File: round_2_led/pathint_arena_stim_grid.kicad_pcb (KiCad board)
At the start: 2 copper layers, 254 x 254 mm, 14 parts, among them J1 conn_2x13_odd_even, M1 0P25_THRU_HOLE, M2 0P25_THRU_HOLE, M3 0P25_THRU_HOLE, M4 0P25_THRU_HOLE

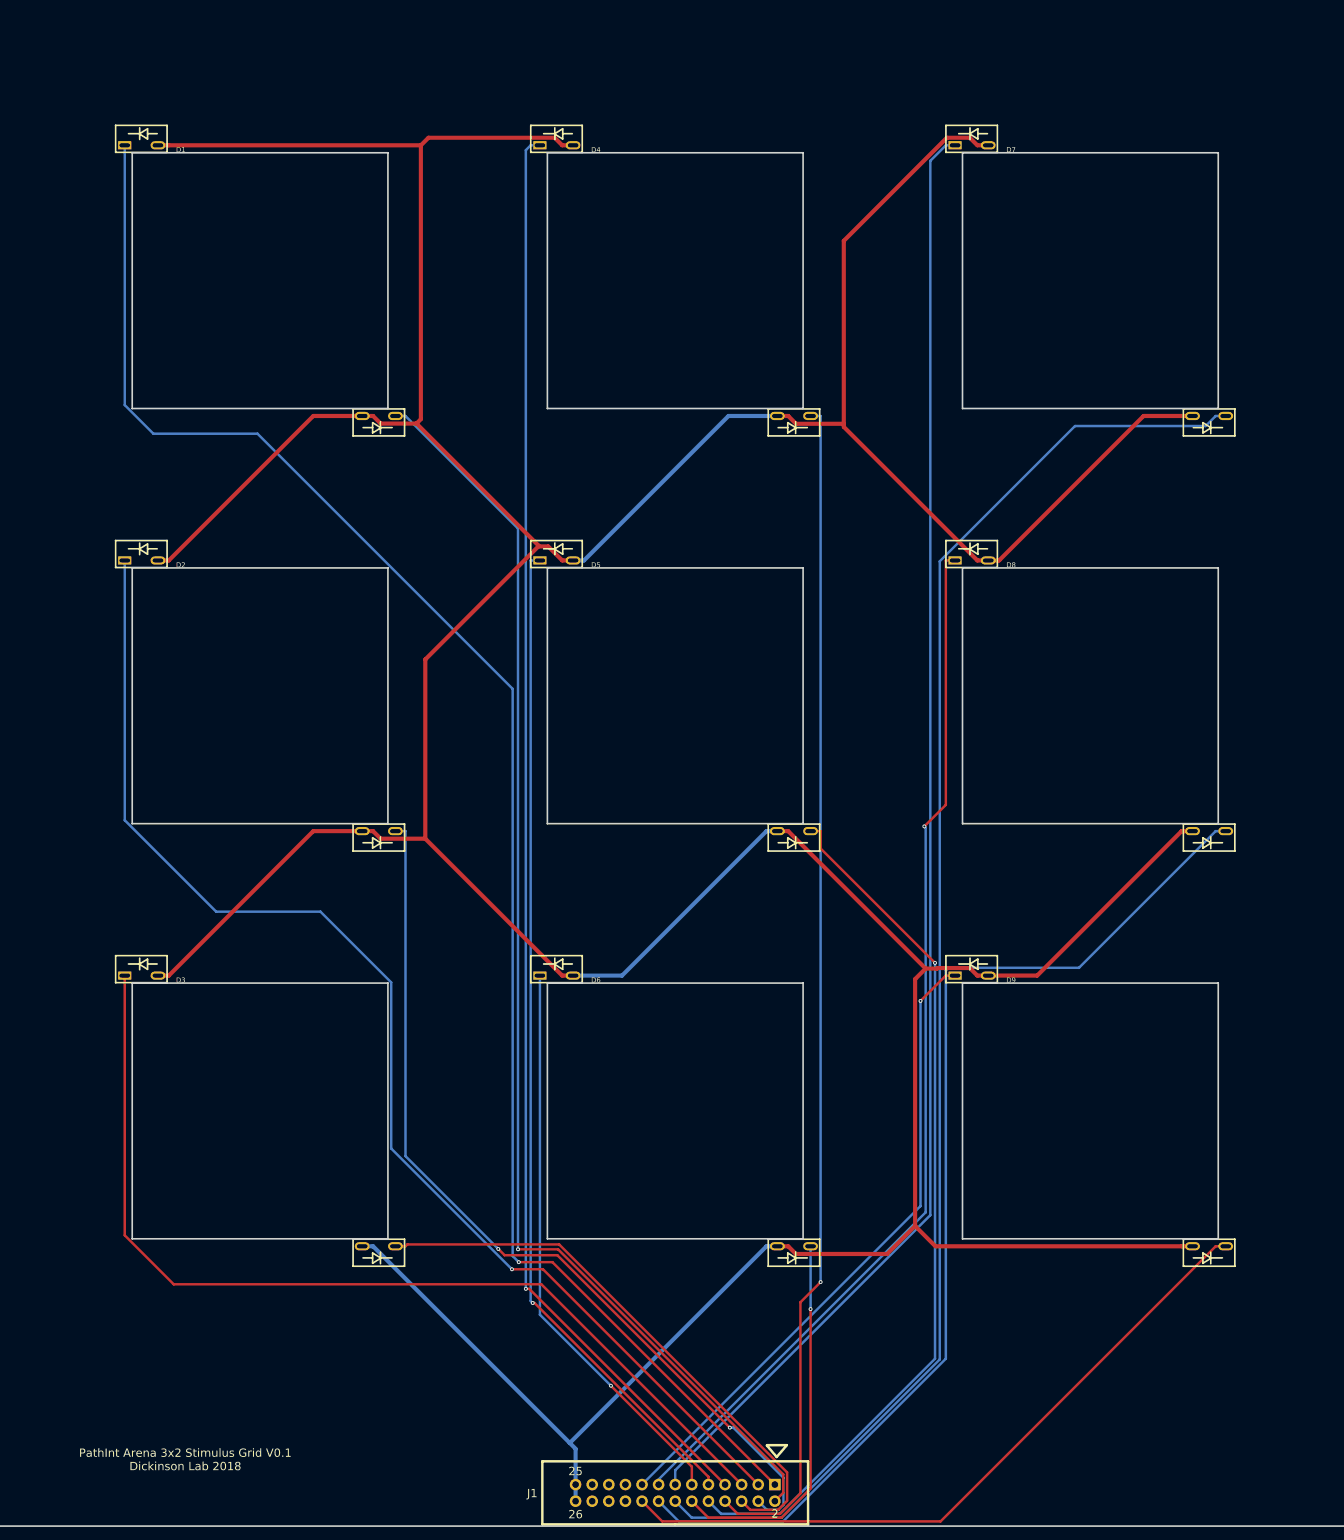
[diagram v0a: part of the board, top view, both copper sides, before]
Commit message: Added new design w/ circular arenas and leds at 60 degree angle.
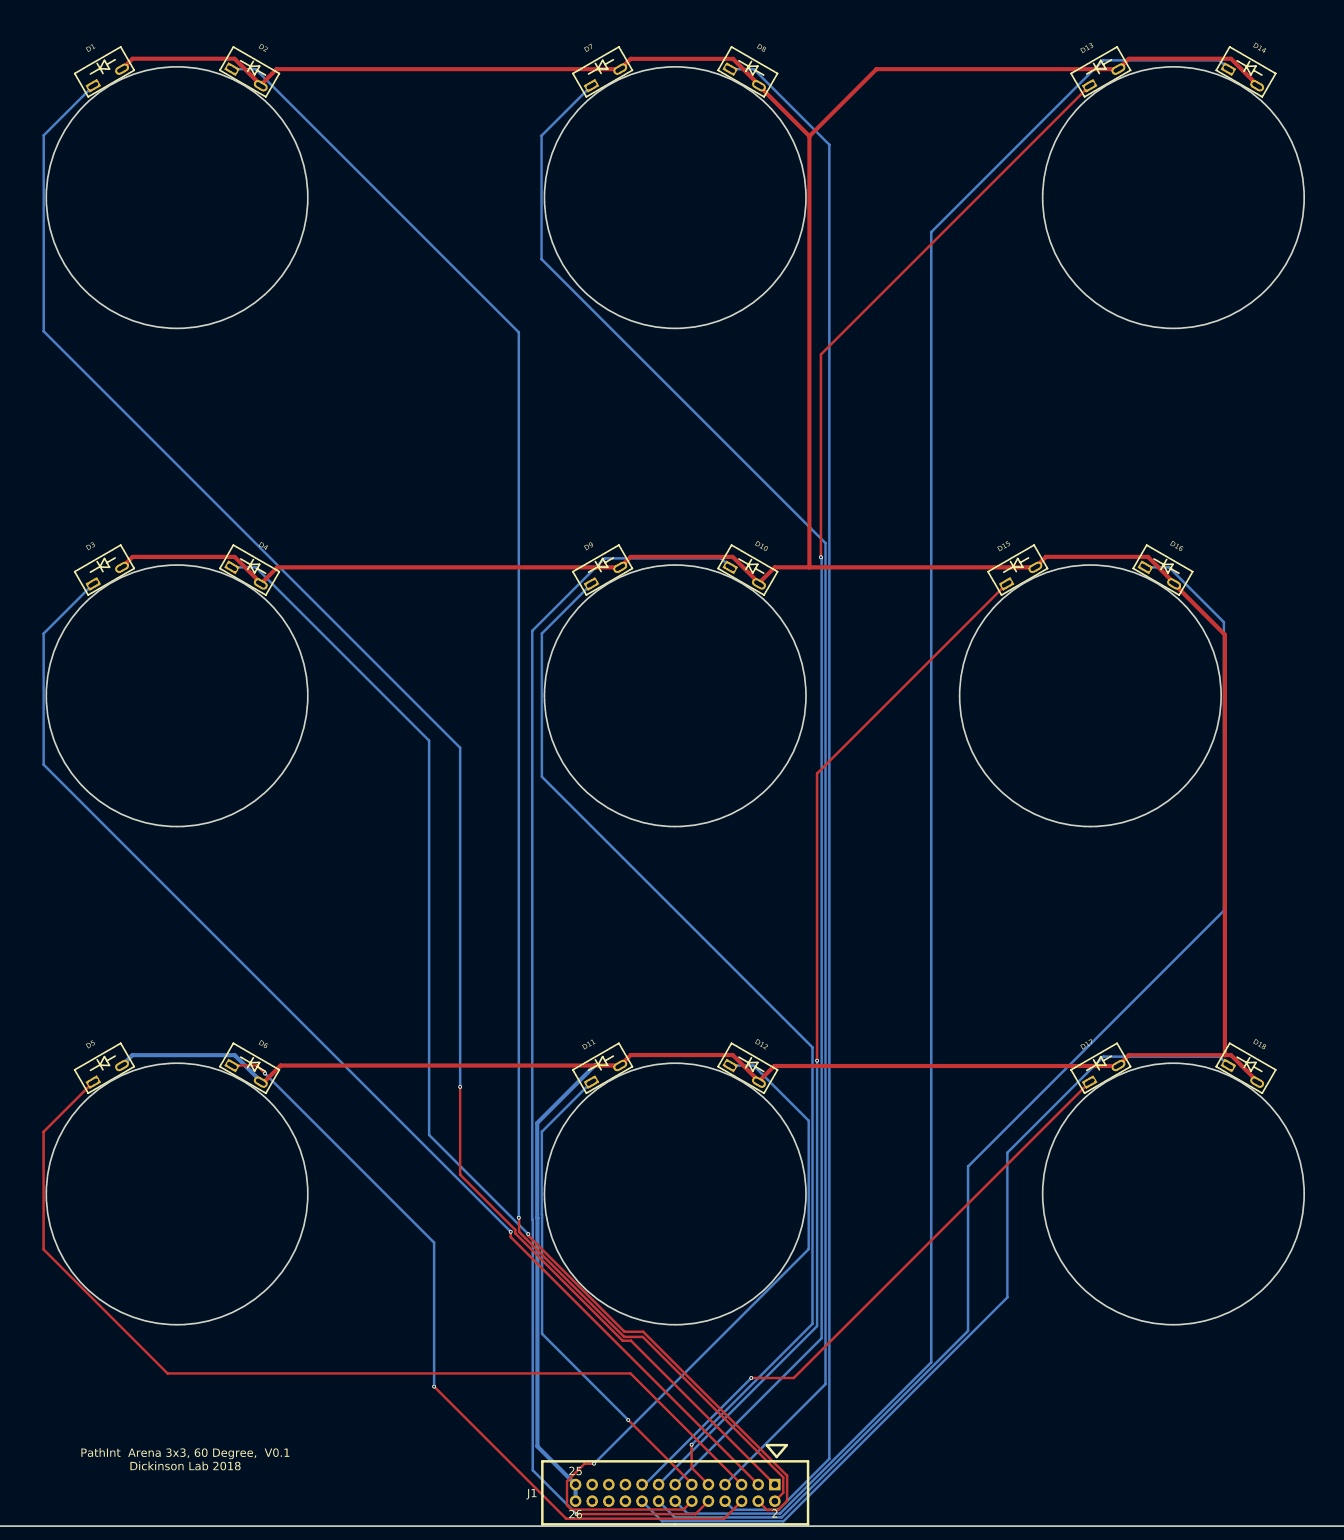
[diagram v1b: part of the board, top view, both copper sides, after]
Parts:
- added D10: ARENA_LED, ARENA_ELEM:SUB_ARENA, F.Cu at (152.4, 152.4)
- added D11, D12: ARENA_LED, ARENA_ELEM:SUB_ARENA, F.Cu at (152.4, 228.6)
- added D13, D14: ARENA_LED, ARENA_ELEM:SUB_ARENA, F.Cu at (228.6, 76.2)
- added D15, D16: ARENA_LED, ARENA_ELEM:SUB_ARENA, F.Cu at (215.9, 152.4)
- added D17, D18: ARENA_LED, ARENA_ELEM:SUB_ARENA, F.Cu at (228.6, 228.6)
- D1, D2, D3, D4, D5, D6, D7, D8, D9: value ARENA_LED_PAIR -> ARENA_LED
- moved D5 107.8 mm to (76.2, 228.6), turned to 30 degrees
- moved D4 99.2 mm to (76.2, 152.4), turned to 330 degrees
- moved D8 99.2 mm to (152.4, 76.2), turned to 330 degrees
- moved D9 89.8 mm to (152.4, 152.4), turned to 30 degrees
- moved D2 77.3 mm to (76.2, 76.2), turned to 330 degrees
- moved D6 77.3 mm to (76.2, 228.6), turned to 330 degrees
- moved D3 64.8 mm to (76.2, 152.4), turned to 30 degrees
- moved D7 64.8 mm to (152.4, 76.2), turned to 30 degrees
- moved D1 18.0 mm to (76.2, 76.2), turned to 30 degrees
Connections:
- D2 pad 1: /PWM2 -> /PWM1
- D3 pad 1: /PWM4 -> /PWM2
- D4 pad 1: /PWM6 -> /PWM3
- D5 pad 1: /PWM8 -> /PWM4
- D6 pad 1: /PWM10 -> /PWM5
- D7 pad 1: /PWM12 -> /PWM6
- D8 pad 1: /PWM14 -> /PWM7
- D9 pad 1: /PWM16 -> /PWM8
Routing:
- net /VIN: track 829.5 -> 760.6 mm
- net /PWM1: track 195.6 -> 258.3 mm
- net /PWM9: track 134.8 -> 194.3 mm
- net /PWM7: track 181.2 -> 240.7 mm, vias 1 -> 0
- net /PWM13: track 226.6 -> 279.3 mm
- net /PWM11: track 58.1 -> 110.4 mm
- net /PWM3: track 138.3 -> 187.3 mm, vias 2 -> 1
- net /PWM5: track 86.9 -> 120.7 mm, vias 0 -> 2
- net /PWM15: track 166.6 -> 200.3 mm
- net /PWM17: track 108.0 -> 133.9 mm
- net /PWM6: track 219.5 -> 241.5 mm, vias 1 -> 0
- net /PWM12: track 223.4 -> 240.3 mm, vias 0 -> 1
- net /PWM10: track 87.5 -> 74.2 mm
- net /PWM8: track 154.2 -> 166.8 mm
- net /PWM2: track 193.6 -> 186.2 mm
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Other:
- outline, holes or cut-outs redrawn
- board text added: "PathInt Arena 3x3, 60 Degree, V0.1 Dickinson Lab 2018"
- board text removed: "PathInt Arena 3x2 Stimulus Grid V0.1 Dickinson Lab 2018"
